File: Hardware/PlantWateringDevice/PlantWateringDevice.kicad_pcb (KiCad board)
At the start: 4 copper layers, 48 x 45 mm, 58 parts, among them J1 USB_B_Micro, J3 Conn_PIC_ICSP_ICD, J4 Conn_01x03_Socket, M1 Motor_DC, Q1 AO3404A, SW1 SW_Push, SW3 SW_Push, SW5 SW_DIP_x02, U2 LM2903, U4 PIC10F202-IOT, U7 SC39-11EWA

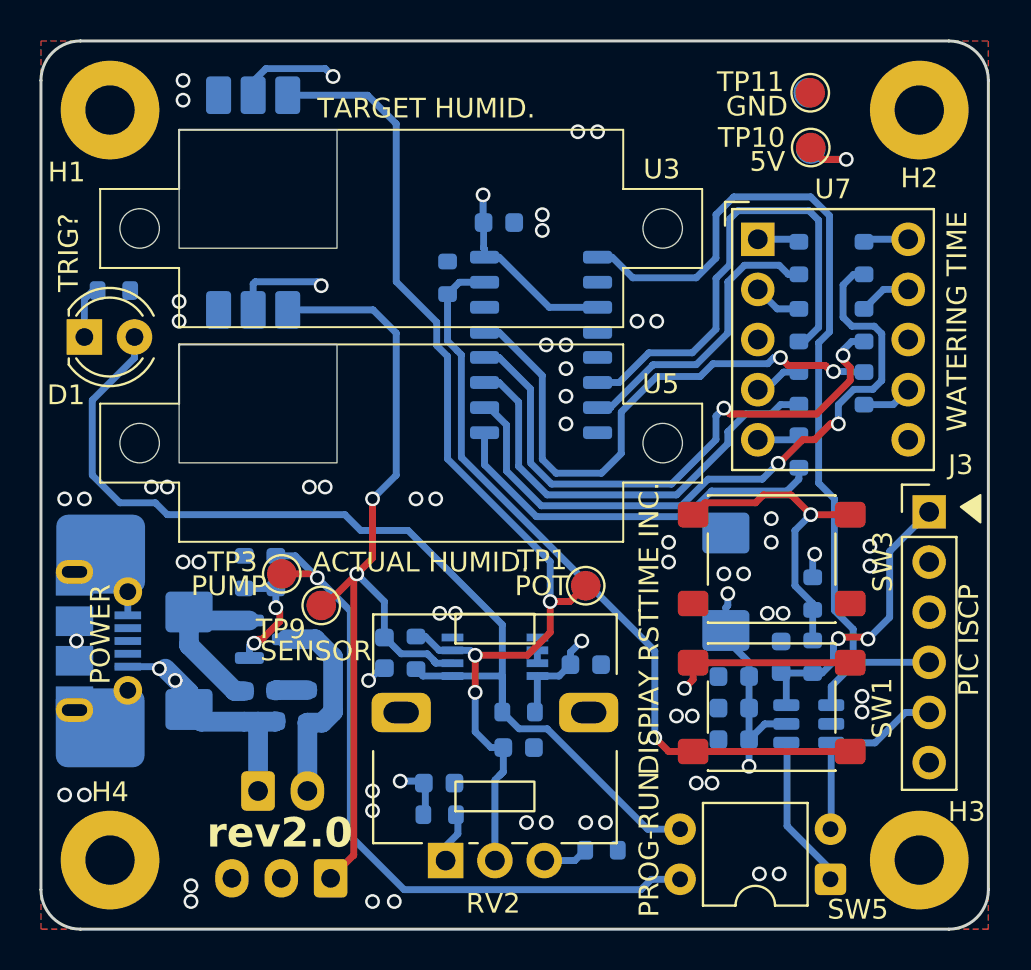
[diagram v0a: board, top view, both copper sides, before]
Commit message: change pcb stackup
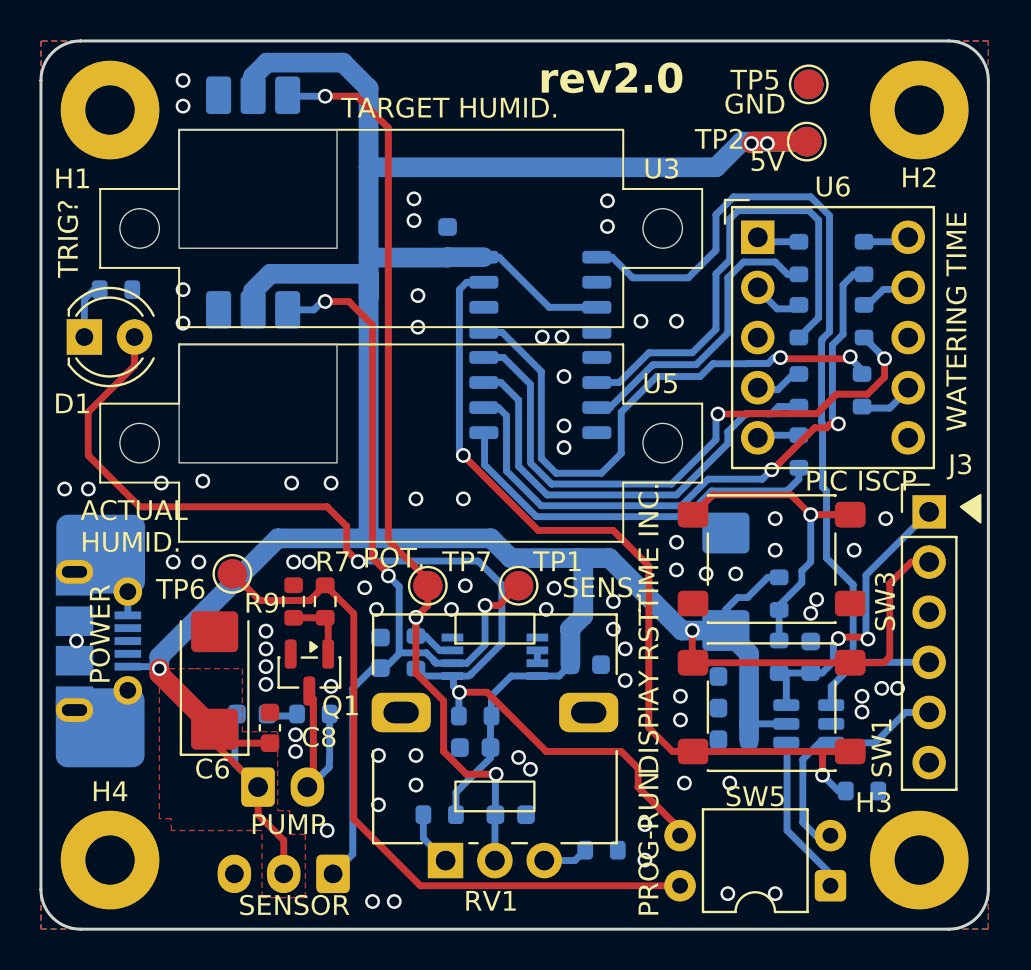
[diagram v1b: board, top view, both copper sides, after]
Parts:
- removed C9: 100u/10v, Capacitor_Tantalum_SMD:CP_EIA-6032-28_Kemet-C
- removed J4: Conn_01x03_Socket, Connector_JST:JST_EH_B3B-EH-A_1x03_P2.50mm_Vertical
- removed R20, R21, R22, R23, R25, R27: 120R, Resistor_SMD:R_0603_1608Metric
- removed R4: 1k, Resistor_SMD:R_0603_1608Metric
- removed RV2: R_Potentiometer, Potentiometer_THT:Potentiometer_Alps_RK09L_Single_Vertical
- removed TP10, TP11, TP12, TP13, TP9: TestPoint, TestPoint:TestPoint_Pad_D1.5mm
- removed U7: SC39-11EWA, Display_7Segment:Sx39-1xxxxx
- added C8: 330n, Capacitor_SMD:C_0603_1608Metric, F.Cu at (146.6, 74.8)
- added J2: Conn_01x03_Socket, Connector_JST:JST_EH_B3B-EH-A_1x03_P2.50mm_Vertical, B.Cu at (149.8, 82.2)
- added R11: 4R7, Resistor_SMD:R_0603_1608Metric, B.Cu at (148.8, 74.1)
- added R15: 120R, Resistor_SMD:R_0603_1608Metric, B.Cu at (176.6, 57.7)
- added R16: 120R, Resistor_SMD:R_0603_1608Metric, B.Cu at (173.4, 60.8)
- added R17: 120R, Resistor_SMD:R_0603_1608Metric, B.Cu at (173.4, 57.7)
- added R18: 120R, Resistor_SMD:R_0603_1608Metric, B.Cu at (173.4, 54.2)
- added R19: 120R, Resistor_SMD:R_0603_1608Metric, B.Cu at (173.4, 51.0)
- added R5: 1k, Resistor_SMD:R_0603_1608Metric, B.Cu at (157.0, 74.2)
- added RV1: R_Potentiometer, Potentiometer_THT:Potentiometer_Alps_RK09L_Single_Vertical, F.Cu at (155.5, 81.5)
- added TP2: TestPoint, TestPoint:TestPoint_Pad_D1.5mm, F.Cu at (173.8, 45.1)
- added TP4: TestPoint, TestPoint:TestPoint_Pad_D1.5mm, B.Cu at (173.9, 42.2)
- added TP5: TestPoint, TestPoint:TestPoint_Pad_D1.5mm, F.Cu at (173.9, 42.2)
- added TP6: TestPoint, TestPoint:TestPoint_Pad_D1.5mm, F.Cu at (144.7, 67.0)
- added TP7: TestPoint, TestPoint:TestPoint_Pad_D1.5mm, F.Cu at (154.6, 67.6)
- added U1: ~, Package_SO:JEITA_SOIC-16_3.9x9.9mm_P1.27mm, B.Cu at (160.3, 55.4)
- C6: value 330n -> 100u/10v; footprint Capacitor_SMD:C_0603_1608Metric -> Capacitor_Tantalum_SMD:CP_EIA-6032-28_Kemet-C; moved to F.Cu
- Q1, R7, R9: moved to F.Cu
- R10: value TBD -> 510R
- R12: value 4R7 -> 10k
- R14: value 10k -> 120R
- R3: value 510R -> TBD
- TP3: moved to B.Cu
- U6: value ~ -> SC39-11EWA; footprint Package_SO:JEITA_SOIC-16_3.9x9.9mm_P1.27mm -> Display_7Segment:Sx39-1xxxxx; moved to F.Cu
- moved TP3 34.5 mm to (173.8, 45.1)
- moved R12 28.4 mm to (176.6, 78.0), turned to 0 degrees
- moved R3 23.9 mm to (154.0, 71.0), turned to 90 degrees
- moved R10 23.9 mm to (138.8, 52.6), turned to 180 degrees
- moved R14 21.2 mm to (176.7, 54.2), turned to -90 degrees
- moved U6 12.3 mm to (171.3, 49.9), turned to 0 degrees
- moved C7 3.96 mm to (158.8, 79.2)
- moved TP1 3.40 mm to (159.2, 67.6)
- moved R13 3.40 mm to (176.7, 51.0)
- moved R7 2.91 mm to (149.4, 68.4)
- moved R9 2.91 mm to (147.8, 68.4)
- moved C4 2.79 mm to (155.6, 50.2), turned to 90 degrees
- moved Q1 2.69 mm to (148.6, 72.0), turned to -90 degrees
- moved C3 2.20 mm to (157.0, 75.8), turned to 180 degrees
- moved C6 1.99 mm to (143.8, 72.4)
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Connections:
- C2 pad 1: HUMIDITY_SENSOR -> /Display/HUMIDITY_SENSOR
- C3 pad 1: POTENTIOMETER_DATA -> +5V
- C7 pad 1: +5V -> /Display/POTENTIOMETER_DATA
- D1 pad 2: HUMIDITY_COMPARATION -> /DataHandling/HUMIDITY_COMPARATION
- J3 pad 4: BARGRAPH_DATA -> /DataHandling/DISPLAY_DATA
- R10 pad 1: HUMIDITY_COMPARATION -> GND
- R10 pad 2: POTENTIOMETER_DATA -> Net-(D1-K)
- R12 pad 1: Net-(M1--) -> Net-(U1-RES)
- R12 pad 2: Net-(C14-Pad2) -> GND
- R13 pad 1: Net-(U7-B) -> Net-(U6-A)
- R13 pad 2: Net-(U6-B) -> Net-(U1-A)
- R14 pad 1: Net-(U6-RES) -> Net-(U6-B)
- R14 pad 2: GND -> Net-(U1-B)
- R3 pad 1: GND -> /DataHandling/HUMIDITY_COMPARATION
- R3 pad 2: Net-(D1-K) -> /Display/POTENTIOMETER_DATA
- R7 pad 2: PUMP_ON_OFF -> /DataHandling/PUMP_ON_OFF
- SW1 pad 1: Net-(U6-RES) -> Net-(U1-RES)
- SW5 pad 3: HUMIDITY_COMPARATION -> /DataHandling/HUMIDITY_COMPARATION
- SW5 pad 4: PUMP_ON_OFF -> /DataHandling/PUMP_ON_OFF
- TP1 pad 1: POTENTIOMETER_DATA -> /Display/HUMIDITY_SENSOR
- TP3 pad 1: PUMP_ON_OFF -> +5V
- U2 pad 1: HUMIDITY_COMPARATION -> /DataHandling/HUMIDITY_COMPARATION
- U2 pad 2: HUMIDITY_SENSOR -> /Display/HUMIDITY_SENSOR
- U2 pad 3: POTENTIOMETER_DATA -> /Display/POTENTIOMETER_DATA
- U3 pad 3: POTENTIOMETER_DATA -> /Display/POTENTIOMETER_DATA
- U4 pad 1: BARGRAPH_DATA -> /DataHandling/DISPLAY_DATA
- U5 pad 3: HUMIDITY_SENSOR -> /Display/HUMIDITY_SENSOR
- U6 pad 1: BARGRAPH_DATA -> Net-(U6-G)
- U6 pad 2: GND -> Net-(U6-F)
- U6 pad 3: +5V -> GND
- U6 pad 4: unconnected-(U6-DEO-Pad4) -> Net-(U6-E)
- U6 pad 5: unconnected-(U6-CO-Pad5) -> Net-(U6-D)
- U6 pad 6: Net-(U6-F) -> unconnected-(U6-DP-Pad6)
- U6 pad 9: Net-(U6-D) -> Net-(U6-B)
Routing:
- net +5V: track 66.2 -> 177.8 mm, vias 12 -> 4
- net /DataHandling/HUMIDITY_COMPARATION: track 0.00 -> 56.7 mm, vias 0 -> 2
- net POTENTIOMETER_DATA: track 56.7 -> 0.00 mm, vias 3 -> 0
- net HUMIDITY_COMPARATION: track 54.0 -> 0.00 mm
- net /Display/POTENTIOMETER_DATA: track 0.00 -> 50.1 mm, vias 0 -> 3
- net BARGRAPH_DATA: track 45.7 -> 0.00 mm
- net HUMIDITY_SENSOR: track 45.4 -> 0.00 mm, vias 2 -> 0
- net /DataHandling/DISPLAY_DATA: track 0.00 -> 45.3 mm
- net Net-(U1-RES): track 0.00 -> 45.3 mm, vias 0 -> 2
- net /Display/HUMIDITY_SENSOR: track 0.00 -> 43.9 mm, vias 0 -> 3
- net Net-(U6-RES): track 39.1 -> 0.00 mm, vias 1 -> 0
- net /DataHandling/PUMP_ON_OFF: track 0.00 -> 36.8 mm
- net PUMP_ON_OFF: track 36.3 -> 0.00 mm, vias 1 -> 0
- net Net-(U6-A): track 34.1 -> 1.85 mm, vias 2 -> 0
- net Net-(U1-A): track 0.00 -> 31.8 mm, vias 0 -> 2
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- added copper zone on F.Cu, net +5V
- added copper zone on In2.Cu, net GND
- removed copper zone on In2.Cu, net +5V
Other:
- board text added: "POT."
- board text added: "SENS."
- board text removed: "POT"
